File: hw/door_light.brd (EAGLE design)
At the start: 32.2 x 34.6 mm, 28 parts, among them IC1 TINY13-20SSU, Q1 BSP250, T2 KP-3216P3C, U1 MC33063ADE4

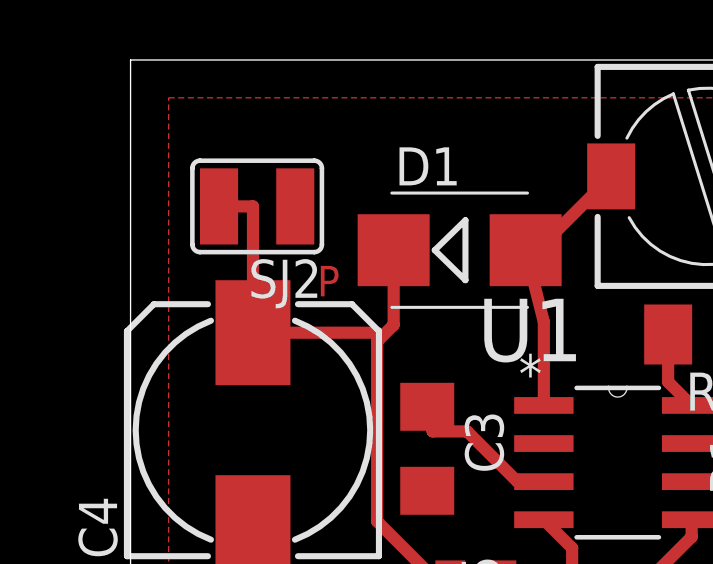
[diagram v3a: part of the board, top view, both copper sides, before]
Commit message: minor alignment update on PCB
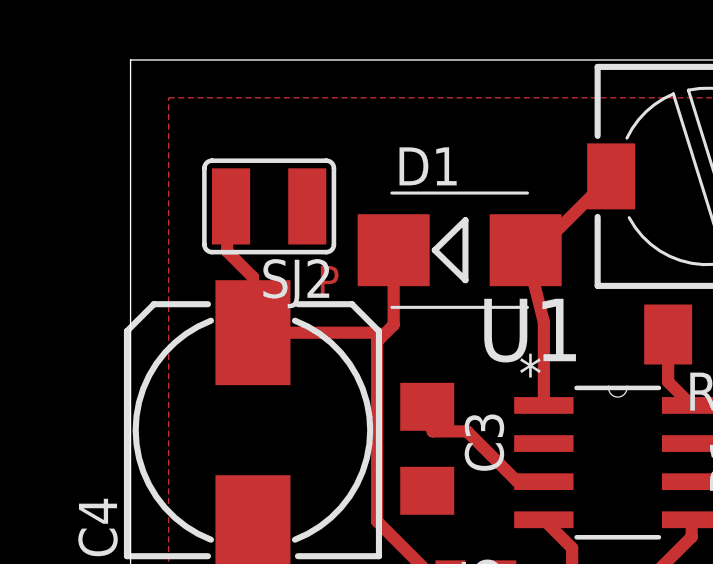
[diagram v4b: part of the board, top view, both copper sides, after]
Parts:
- moved SJ2 0.40 mm to (22.4, 69.5)
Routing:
- net +12V: track 23.8 -> 21.5 mm
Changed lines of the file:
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@@
 </element>
 <element name="SJ1" library="jumper" package="SJW" value="PWR" x="47" y="53" rot="R90"/>
-<element name="SJ2" library="jumper" package="SJW" value="LIGHT" x="22" y="69.5" rot="R180"/>
+<element name="SJ2" library="jumper" package="SJW" value="LIGHT" x="22.4" y="69.5" rot="R180"/>
 </elements>
 <signals>
@@
 <contactref element="C4" pad="+"/>
 <contactref element="R4" pad="2"/>
-<wire x1="21.86" y1="65.29" x2="21.86" y2="66.86" width="0.4064" layer="1"/>
+<wire x1="21.86" y1="65.29" x2="21.86" y2="67.14" width="0.4064" layer="1"/>
 <wire x1="26.55" y1="65.55" x2="26" y2="65" width="0.4064" layer="1"/>
 <wire x1="26" y1="65" x2="26" y2="59" width="0.4064" layer="1"/>
@@
 <wire x1="27.85" y1="57.15" x2="26" y2="59" width="0.4064" layer="1"/>
 <contactref element="SJ2" pad="2"/>
-<wire x1="20.73" y1="69.5" x2="21.86" y2="69.5" width="0.4064" layer="1"/>
-<wire x1="21.86" y1="69.5" x2="21.86" y2="65.29" width="0.4064" layer="1"/>
 <wire x1="21.86" y1="65.29" x2="26" y2="65.29" width="0.4064" layer="1"/>
 <wire x1="26" y1="65.29" x2="26" y2="65" width="0.4064" layer="1"/>
+<wire x1="21.86" y1="67.14" x2="21" y2="68" width="0.4064" layer="1"/>
+<wire x1="21" y1="68" x2="21" y2="69.37" width="0.4064" layer="1"/>
+<wire x1="21" y1="69.37" x2="21.13" y2="69.5" width="0.4064" layer="1"/>
 </signal>
 <signal name="N$2">
